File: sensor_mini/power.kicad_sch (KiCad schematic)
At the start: 14 parts, among them J1 Conn_01x05_Female, U1 INA180, U2 INA180, U3 SPU01M-15, U4 MIC5365-3.3

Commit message: Clean Up
Removed old files
Cleaned up Schematics
Created new PDFs
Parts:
- added C17: 4.7uF, Capacitor_SMD:C_0805_2012Metric_Pad1.18x1.45mm_HandSolder, symbol Device:C
- R8: renamed from R1; value 200mR -> 0.2 Ω
- R9: renamed from R2; value 200mR -> 0.2 Ω
- renumbered C1 to C14, C2 to C15, C3 to C16, C4 to C18, C5 to C19, J1 to J4, U1 to U6, U2 to U7, U3 to U8, U4 to U9
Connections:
- net +12V: now also C17.1
- net GND: now also C17.2
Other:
- moved on the sheet: C14, C15, C16, C18, C19, F1, F2, J4, R8, R9, U6, U7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

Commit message: Clean Up
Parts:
- R8, R9: value 0.2 Ω -> 200mR
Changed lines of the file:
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@@
     (in_bom yes) (on_board yes)
     (property "Reference" "R8" (id 0) (at 82.55 98.933 90))
-    (property "Value" "0.2 Ω" (id 1) (at 82.55 101.2444 90))
+    (property "Value" "200mR" (id 1) (at 82.55 101.2444 90))
     (property "Footprint" "Resistor_SMD:R_1206_3216Metric_Pad1.42x1.75mm_HandSolder" (id 2) (at 82.296 105.156 90)
       (effects (font (size 1.27 1.27)) hide)
@@
     (in_bom yes) (on_board yes)
     (property "Reference" "R9" (id 0) (at 82.55 37.973 90))
-    (property "Value" "0.2 Ω" (id 1) (at 82.55 40.2844 90))
+    (property "Value" "200mR" (id 1) (at 82.55 40.2844 90))
     (property "Footprint" "Resistor_SMD:R_1206_3216Metric_Pad1.42x1.75mm_HandSolder" (id 2) (at 82.296 44.196 90)
       (effects (font (size 1.27 1.27)) hide)

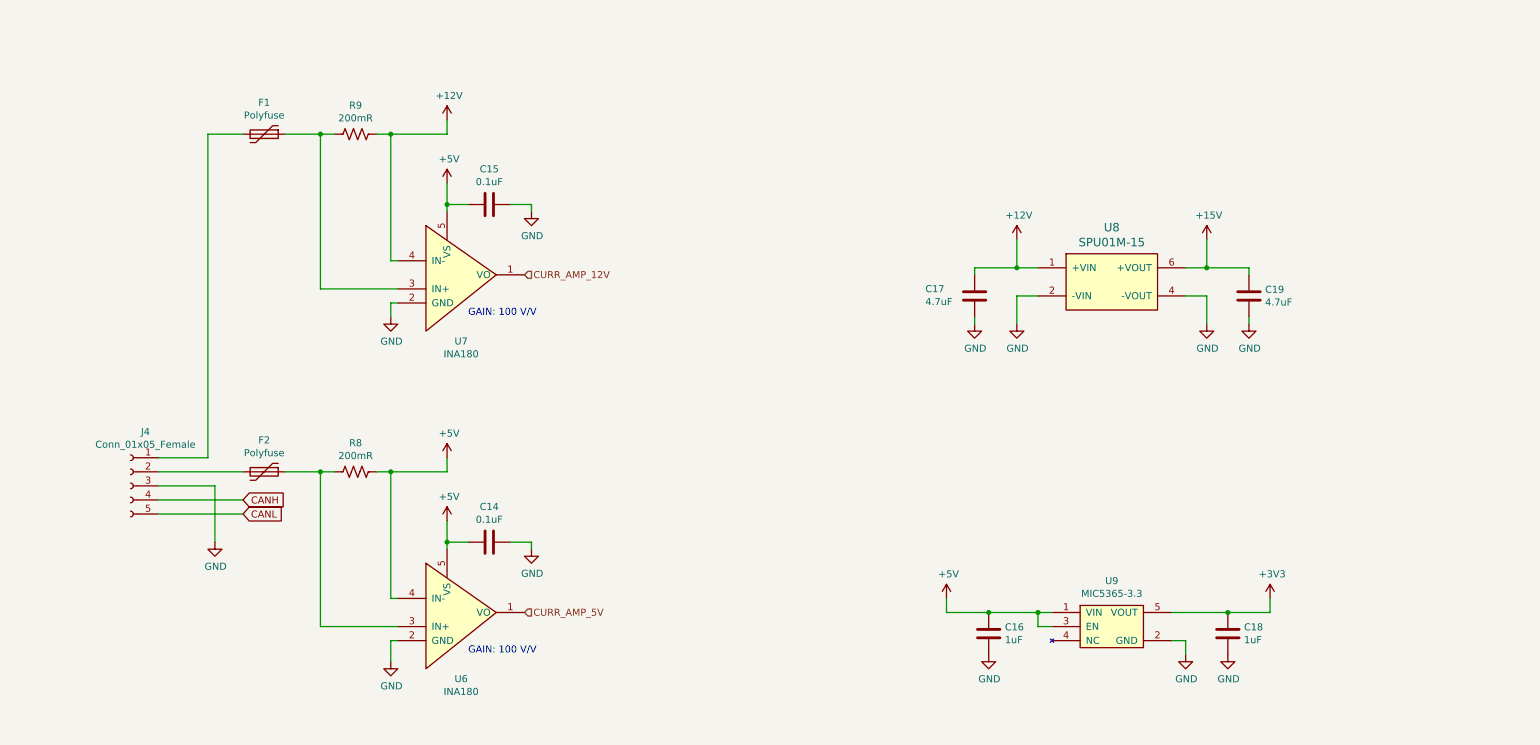
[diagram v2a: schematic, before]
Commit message: Finish Analog Sensors Schematic
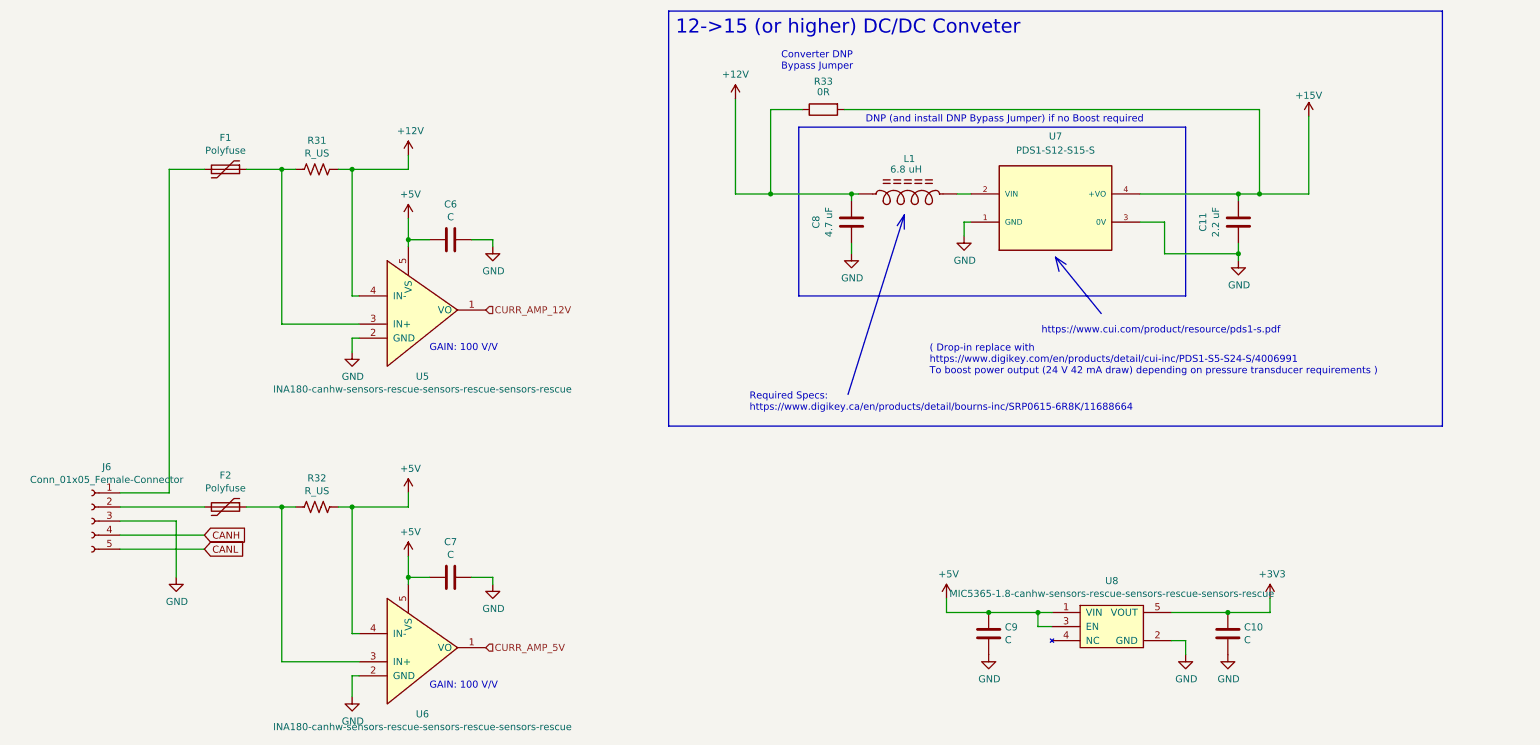
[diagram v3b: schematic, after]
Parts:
- removed C17: 4.7uF, Capacitor_SMD:C_0805_2012Metric_Pad1.18x1.45mm_HandSolder, symbol Device:C
- removed C19: 4.7uF, Capacitor_SMD:C_0805_2012Metric_Pad1.15x1.40mm_HandSolder, symbol Device:C
- removed U8: SPU01M-15, flight_instr:SIP6_Housing, symbol flight_instr:SPU01M-15
- added C11: 2.2 uF, Capacitor_SMD:C_0805_2012Metric_Pad1.15x1.40mm_HandSolder, symbol Device:C
- added C8: 4.7 uF, Capacitor_SMD:C_0805_2012Metric_Pad1.15x1.40mm_HandSolder, symbol Device:C
- added L1: 6.8 uH, symbol bourns_SRP0615_inductors:L_POWER_SHIELDED
- added R33: 0R, symbol Device:R
- added U7: PDS1-S12-S15-S, CONV_PDS1-S12-S15-S, symbol PDS1-S12-S15-S:PDS1-S12-S15-S
- C10: renamed from C18; value 1uF -> C
- C6: renamed from C15; value 0.1uF -> C
- C7: renamed from C14; value 0.1uF -> C
- C9: renamed from C16; value 1uF -> C
- J6: renamed from J4; value Conn_01x05_Female -> Conn_01x05_Female-Connector
- R31: renamed from R9; value 200mR -> R_US
- R32: renamed from R8; value 200mR -> R_US
- U5: renamed from U7; value INA180 -> INA180-canhw-sensors-rescue-sensors-rescue-sensors-rescue
- U6: value INA180 -> INA180-canhw-sensors-rescue-sensors-rescue-sensors-rescue
- U8: renamed from U9; value MIC5365-3.3 -> MIC5365-1.8-canhw-sensors-rescue-sensors-rescue-sensors-rescue
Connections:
- net +12V: now also C8.1, L1., R33.1
- net +15V: now also C11.1, R33.2, U7.4 (+VO)
- net GND: now also C11.2, C8.2, U7.1 (GND), U7.3 (0V)
- new net: L1., U7.2 (VIN)
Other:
- note added: "( Drop-in replace with https://www.digikey.com/en/products/detail/cui-inc/PDS1-S5-S24-S/4006991 To boost power output (24 V 42 mA draw) depending on pressure transducer requirements )"
- note added: "12->15 (or higher) DC/DC Conveter"
- note added: "Converter DNP Bypass Jumper"
- note added: "DNP (and install DNP Bypass Jumper) if no Boost required"
- note added: "Required Specs: https://www.digikey.ca/en/products/detail/bourns-inc/SRP0615-6R8K/11688664"
- note added: "https://www.cui.com/product/resource/pds1-s.pdf"
- moved on the sheet: C6, C7, F1, F2, J6, R31, R32, U5, U6

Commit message: Added Test Points For the People
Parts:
- added TP? (x6): 5000, KEYSTONE_5000, symbol Keysight_5000_testpoints:5000
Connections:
- net +12V: now also TP?.1
- net +15V: now also TP?.1
- net +3V3: now also TP?.1
- net +5V: now also TP?.1
- net CURR_AMP_12V: now also TP?.1
- net CURR_AMP_5V: now also TP?.1

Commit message: Clean up the festering cesspool that was the minisensor folder
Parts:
- removed U5: INA180-canhw-sensors-rescue-sensors-rescue-sensor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, Package_TO_SOT_SMD:SOT-23-5_HandSoldering, symbol sensors-rescue:INA180-canhw-sensors-rescue-sensors-rescue-sensors-rescue
- added U5: INA180, Package_TO_SOT_SMD:SOT-23-5_HandSoldering, symbol canhw:INA180
- J6: symbol sensors-rescue:Conn_01x05_Female-Connector -> Connector:Conn_01x05_Female
- U6: value INA180-canhw-sensors-rescue-sensors-rescue-sensors-rescue -> INA180; symbol sensors-rescue:INA180-canhw-sensors-rescue-sensors-rescue-sensors-rescue -> canhw:INA180
- U8: value MIC5365-1.8-canhw-sensors-rescue-sensors-rescue-sensors-rescue -> MIC5365-1.8; symbol sensors-rescue:MIC5365-1.8-canhw-sensors-rescue-sensors-rescue-sensors-rescue -> canhw:MIC5365-1.8
- gave numbers to parts that had none: 6
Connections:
- net +12V: now also U5.4 (IN-)
- net +5V: now also U5.5 (VS)
- net CURR_AMP_12V: now also U5.1 (VO)
- net GND: now also U5.2 (GND)
- net at F1.1, R31.2: now also U5.3 (IN+)
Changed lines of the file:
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@@
     (pin "1")
   )
-  (symbol (lib_id "sensors-rescue:INA180-canhw-sensors-rescue-sensors-rescue-sensors-rescue") (at 95.885 135.89 0) (unit 1)
+  (symbol (lib_id "canhw:INA180") (at 95.885 135.89 0) (unit 1)
     (in_bom yes) (on_board yes)
     (property "Reference" "U6" (id 0) (at 94.615 147.8788 0))
-    (property "Value" "INA180-canhw-sensors-rescue-sensors-rescue-sensors-rescue" (id 1) (at 94.615 150.1902 0))
+    (property "Value" "INA180" (id 1) (at 94.615 150.1902 0))
     (property "Footprint" "Package_TO_SOT_SMD:SOT-23-5_HandSoldering" (id 2) (at 95.885 135.89 0)
       (effects (font (size 1.27 1.27)) hide)
     )
-    (property "Datasheet" "" (id 3) (at 95.885 135.89 0)
+    (property "Datasheet" "http://www.ti.com/lit/ds/symlink/ina180.pdf" (id 3) (at 95.885 135.89 0)
       (effects (font (size 1.27 1.27)) hide)
     )
@@
     (pin "1")
   )
-  (symbol (lib_id "sensors-rescue:Conn_01x05_Female-Connector") (at 34.925 113.03 0) (mirror y) (unit 1)
+  (symbol (lib_id "Connector:Conn_01x05_Female") (at 34.925 113.03 0) (mirror y) (unit 1)
     (in_bom yes) (on_board yes)
     (property "Reference" "J6" (id 0) (at 37.6174 103.251 0))
@@
     (pin "1")
   )
-  (symbol (lib_id "sensors-rescue:MIC5365-1.8-canhw-sensors-rescue-sensors-rescue-sensors-rescue") (at 219.71 129.54 0) (unit 1)
+  (symbol (lib_id "canhw:MIC5365-1.8") (at 219.71 129.54 0) (unit 1)
     (in_bom yes) (on_board yes)
     (property "Reference" "U8" (id 0) (at 219.075 123.825 0))
-    (property "Value" "MIC5365-1.8-canhw-sensors-rescue-sensors-rescue-sensors-rescue" (id 1) (at 219.075 126.1364 0))
+    (property "Value" "MIC5365-1.8" (id 1) (at 219.075 126.1364 0))
     (property "Footprint" "Package_TO_SOT_SMD:SOT-23-5_HandSoldering" (id 2) (at 220.98 129.54 0)
       (effects (font (size 1.27 1.27)) hide)
     )
-    (property "Datasheet" "" (id 3) (at 220.98 129.54 0)
-      (effects (font (size 1.27 1.27)) hide)
-    )
-    (pin "1")
-    (pin "2")
-    (pin "3")
-    (pin "4")
-    (pin "5")
-  )
-  (symbol (lib_id "sensors-rescue:INA180-canhw-sensors-rescue-sensors-rescue-sensors-rescue") (at 95.885 74.93 0) (unit 1)
-    (in_bom yes) (on_board yes)
-    (property "Reference" "U5" (id 0) (at 94.615 86.9188 0))
-    (property "Value" "INA180-canhw-sensors-rescue-sensors-rescue-sensors-rescue" (id 1) (at 94.615 89.2302 0))
-    (property "Footprint" "Package_TO_SOT_SMD:SOT-23-5_HandSoldering" (id 2) (at 95.885 74.93 0)
-      (effects (font (size 1.27 1.27)) hide)
-    )
-    (property "Datasheet" "" (id 3) (at 95.885 74.93 0)
+    (property "Datasheet" "http://ww1.microchip.com/downloads/en/DeviceDoc/mic5365.pdf" (id 3) (at 220.98 129.54 0)
       (effects (font (size 1.27 1.27)) hide)
     )
@@
   (symbol (lib_id "Keysight_5000_testpoints:5000") (at 104.775 39.37 90) (unit 1)
     (in_bom yes) (on_board yes)
-    (property "Reference" "TP?" (id 0) (at 106.045 35.56 0)
+    (property "Reference" "TP14" (id 0) (at 106.045 35.56 0)
       (effects (font (size 1.27 1.27)) (justify left))
     )
@@
   (symbol (lib_id "Keysight_5000_testpoints:5000") (at 116.84 63.5 90) (unit 1)
     (in_bom yes) (on_board yes)
-    (property "Reference" "TP?" (id 0) (at 118.11 59.69 0)
+    (property "Reference" "TP16" (id 0) (at 118.11 59.69 0)
       (effects (font (size 1.27 1.27)) (justify left))
     )
@@
   (symbol (lib_id "Keysight_5000_testpoints:5000") (at 116.205 121.92 90) (unit 1)
     (in_bom yes) (on_board yes)
-    (property "Reference" "TP?" (id 0) (at 117.475 118.11 0)
+    (property "Reference" "TP15" (id 0) (at 117.475 118.11 0)
       (effects (font (size 1.27 1.27)) (justify left))
     )
@@
   (symbol (lib_id "Keysight_5000_testpoints:5000") (at 260.985 121.92 90) (unit 1)
     (in_bom yes) (on_board yes)
-    (property "Reference" "TP?" (id 0) (at 262.255 118.11 0)
+    (property "Reference" "TP17" (id 0) (at 262.255 118.11 0)
       (effects (font (size 1.27 1.27)) (justify left))
     )
@@
   (symbol (lib_id "Keysight_5000_testpoints:5000") (at 100.965 101.6 90) (unit 1)
     (in_bom yes) (on_board yes)
-    (property "Reference" "TP?" (id 0) (at 102.235 97.79 0)
+    (property "Reference" "TP13" (id 0) (at 102.235 97.79 0)
       (effects (font (size 1.27 1.27)) (justify left))
     )
@@
     )
     (pin "1")
+  )
+  (symbol (lib_id "canhw:INA180") (at 95.885 74.93 0) (unit 1)
+    (in_bom yes) (on_board yes)
+    (property "Reference" "U5" (id 0) (at 94.615 86.9188 0))
+    (property "Value" "INA180" (id 1) (at 94.615 89.2302 0))
+    (property "Footprint" "Package_TO_SOT_SMD:SOT-23-5_HandSoldering" (id 2) (at 95.885 74.93 0)
+      (effects (font (size 1.27 1.27)) hide)
+    )
+    (property "Datasheet" "http://www.ti.com/lit/ds/symlink/ina180.pdf" (id 3) (at 95.885 74.93 0)
+      (effects (font (size 1.27 1.27)) hide)
+    )
+    (pin "1")
+    (pin "2")
+    (pin "3")
+    (pin "4")
+    (pin "5")
   )
   (symbol (lib_id "power:+12V") (at 151.13 36.83 0) (unit 1)
@@
   (symbol (lib_id "Keysight_5000_testpoints:5000") (at 265.43 46.355 90) (unit 1)
     (in_bom yes) (on_board yes)
-    (property "Reference" "TP?" (id 0) (at 266.7 42.545 0)
-      (effects (font (size 1.27 1.27)) (justify left))
-    )
+    (property "Reference" "TP18" (id 0) (at 266.7 42.545 0)
+      (effects (font (size 1.27 1.27)) (justify left))
+    )

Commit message: Clean up schematic, add trims on bridge legs
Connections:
- net +15V renamed 12/15V_PWR
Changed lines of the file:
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@@
   (junction (at 109.22 74.93) (diameter 0) (color 0 0 0 0)
   )
-  (wire (pts (xy 254.635 40.005) (xy 254.635 53.975))
-    (stroke (width 0) (type default) (color 0 0 0 0))
-  )
   (wire (pts (xy 108.585 132.08) (xy 116.205 132.08))
     (stroke (width 0) (type default) (color 0 0 0 0))
@@
     (stroke (width 0) (type default) (color 0 0 0 0))
   )
+  (wire (pts (xy 254.635 31.115) (xy 254.635 53.975))
+    (stroke (width 0) (type default) (color 0 0 0 0))
+  )
   (polyline (pts (xy 162.56 41.91) (xy 162.56 72.39))
     (stroke (width 0) (type default) (color 0 0 0 0))
@@
   )
   (wire (pts (xy 83.185 80.01) (xy 81.915 80.01))
+    (stroke (width 0) (type default) (color 0 0 0 0))
+  )
+  (wire (pts (xy 254.635 31.115) (xy 259.08 31.115))
     (stroke (width 0) (type default) (color 0 0 0 0))
   )
@@
   (text "12->15 (or higher) DC/DC Conveter" (at 140.335 25.4 0)
     (effects (font (size 2.54 2.54)) (justify left bottom))
+  )
+  (global_label "12{slash}15V_PWR" (shape input) (at 259.08 31.115 0) (fields_autoplaced)
+    (effects (font (size 1.27 1.27)) (justify left))
+    (property "Intersheet References" "${INTERSHEET_REFS}" (id 0) (at 273.6204 31.0356 0)
+      (effects (font (size 1.27 1.27)) (justify left) hide)
+    )
   )
   (global_label "CANH" (shape input) (at 55.245 115.57 0) (fields_autoplaced)
@@
     )
     (pin "1")
-  )
-  (symbol (lib_id "power:+15V") (at 254.635 40.005 0) (unit 1)
-    (in_bom yes) (on_board yes)
-    (property "Reference" "#PWR055" (id 0) (at 254.635 43.815 0)
-      (effects (font (size 1.27 1.27)) hide)
-    )
-    (property "Value" "+15V" (id 1) (at 254.635 36.195 0))
-    (property "Footprint" "" (id 2) (at 254.635 40.005 0)
-      (effects (font (size 1.27 1.27)) hide)
-    )
-    (property "Datasheet" "" (id 3) (at 254.635 40.005 0)
-      (effects (font (size 1.27 1.27)) hide)
-    )
-    (pin "1")

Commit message: Begin addressing PR comments
Added values, replaced 5->3.3regulator, added decoupling caps, fixed barometer address, accommodated 3-pin connectors, added LEDs, addedd interrupt pin, changed inductor formatting
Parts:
- removed C9: C, Capacitor_SMD:C_0805_2012Metric_Pad1.15x1.40mm_HandSolder, symbol Device:C
- removed U8: MIC5365-1.8, Package_TO_SOT_SMD:SOT-23-5_HandSoldering, symbol canhw:MIC5365-1.8
- added C12: 10 nF, Capacitor_SMD:C_0805_2012Metric_Pad1.15x1.40mm_HandSolder, symbol Device:C
- added C13: 1 uF, Capacitor_SMD:C_0805_2012Metric_Pad1.15x1.40mm_HandSolder, symbol Device:C
- added U8: SPX3819M5-L-3-3, Package_TO_SOT_SMD:SOT-23-5, symbol Regulator_Linear:SPX3819M5-L-3-3
- C10: value C -> 1 uF
- C6, C7: value C -> 0.1 uF
- L1: value 6.8 uH -> SRP0615-6R8K
- R31, R32: value R_US -> 200 mR
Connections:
- net +3V3: now also C13.1, U8.5 (OUT); no longer C10.1
- net +5V: now also C10.1, U8.1 (IN), U8.3 (EN)
- net GND: now also C12.2, C13.2, U8.2 (GND)
- new net: C12.1, U8.4 (BP)
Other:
- note added: "6.8 uH shielded inductor. Required Specs: https://www.digikey.ca/en/products/detail/bourns-inc/SRP0615-6R8K/11688664"
- note removed: "Required Specs: https://www.digikey.ca/en/products/detail/bourns-inc/SRP0615-6R8K/11688664"
